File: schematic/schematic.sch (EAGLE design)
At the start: 6 parts, among them IC1 MEGA8-P

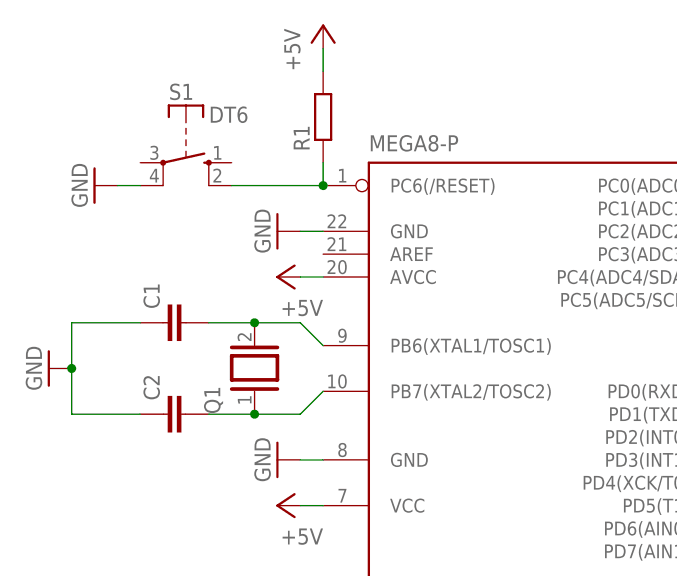
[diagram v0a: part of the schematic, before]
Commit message: Bad at saving schematics - minor update mainly for values
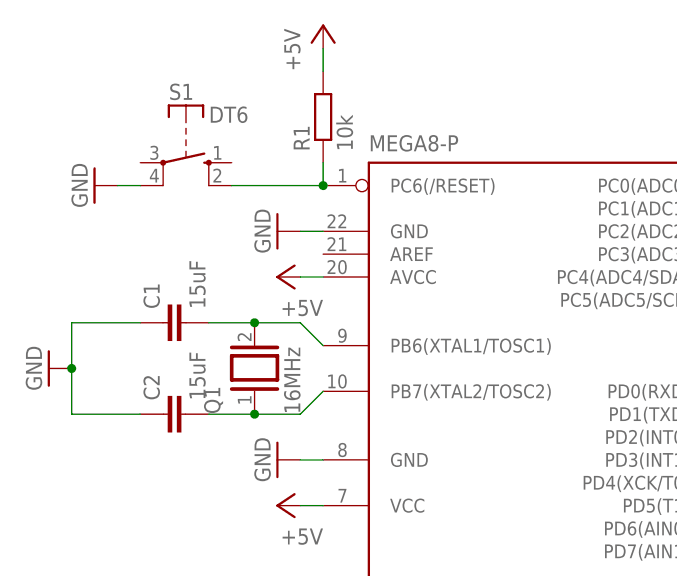
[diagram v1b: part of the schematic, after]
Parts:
- C1, C2: value (none) -> 15uF
- Q1: value (none) -> 16MHz
- R1: value (none) -> 10k
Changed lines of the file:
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@@
 <part name="GND2" library="supply1" deviceset="GND" device=""/>
 <part name="GND3" library="supply1" deviceset="GND" device=""/>
-<part name="Q1" library="special" deviceset="XTAL" device=""/>
-<part name="C1" library="rcl" deviceset="C-EU" device="025-024X044"/>
-<part name="C2" library="rcl" deviceset="C-EU" device="025-024X044"/>
+<part name="Q1" library="special" deviceset="XTAL" device="" value="16MHz"/>
+<part name="C1" library="rcl" deviceset="C-EU" device="025-024X044" value="15uF"/>
+<part name="C2" library="rcl" deviceset="C-EU" device="025-024X044" value="15uF"/>
 <part name="P+3" library="supply1" deviceset="+5V" device=""/>
 <part name="GND4" library="supply1" deviceset="GND" device=""/>
-<part name="R1" library="rcl" deviceset="R-EU_" device="0204/7"/>
+<part name="R1" library="rcl" deviceset="R-EU_" device="0204/7" value="10k"/>
 <part name="S1" library="switch-misc" deviceset="DT" device="6"/>
 </parts>

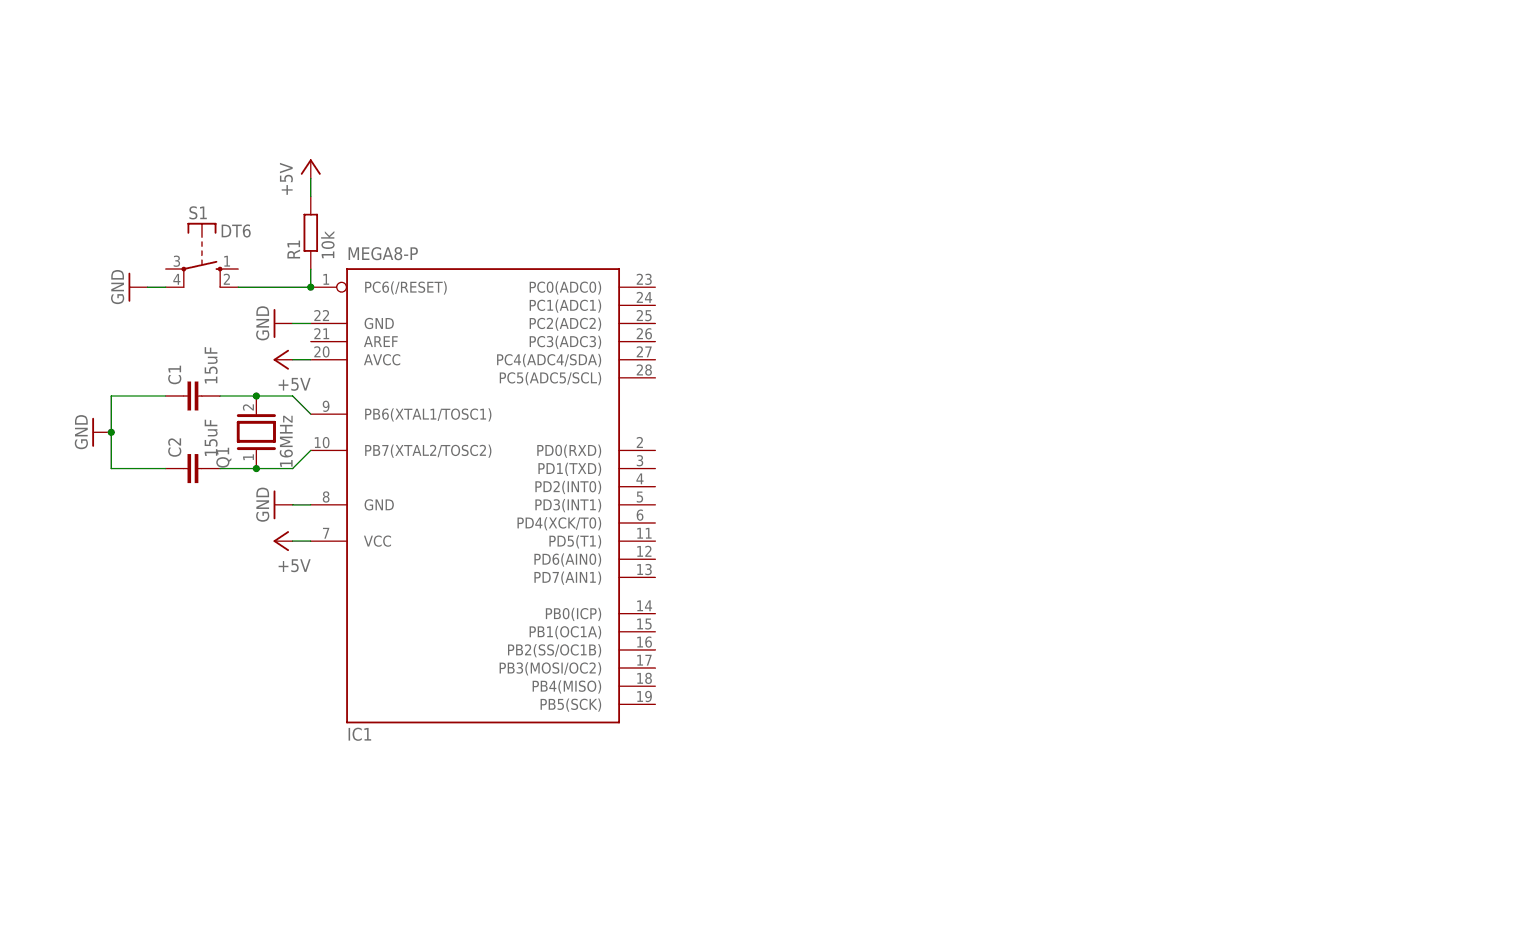
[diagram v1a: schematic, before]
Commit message: Voltage change, Add a host of new subsystems
Critical change: 5V to 3V3, which is slightly out of ratings for 16MHz

Additionally:
* Input buttons
* ICSP Header
* Expansion Header
* SD Card
* Labels
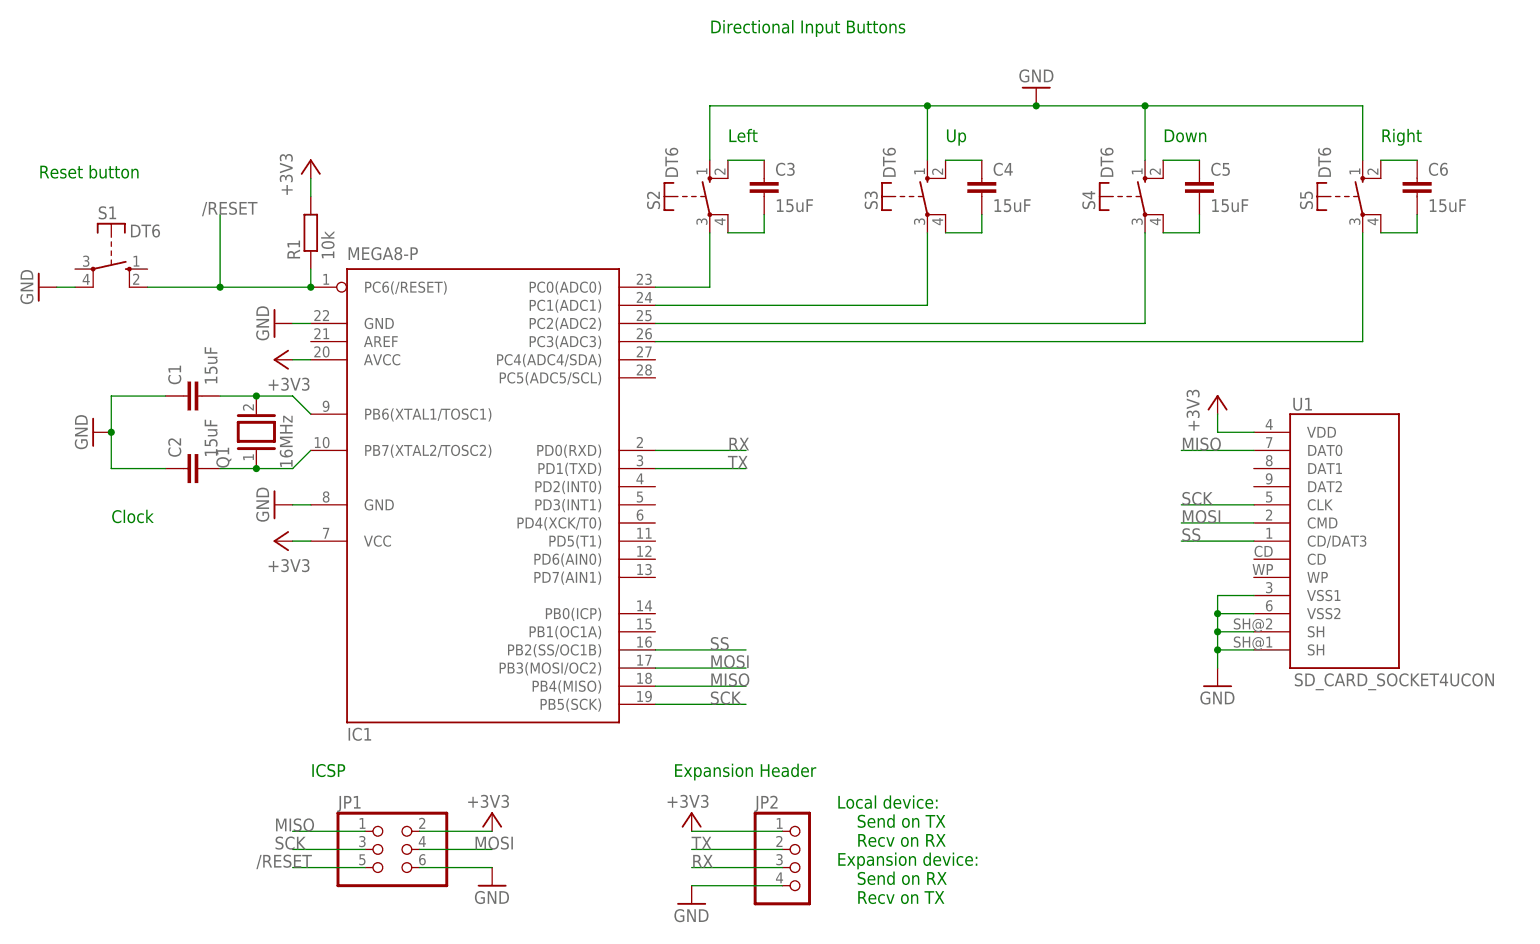
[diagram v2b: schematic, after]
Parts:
- added C3, C4, C5, C6: 15uF, rcl:C-EU025-024X044
- added JP1: (no value), pinhead:PINHD-2X3
- added JP2: (no value), pinhead:PINHD-1X4
- added S2, S3, S4, S5: DT6, switch-misc:DT6
- added U1: SD_CARD_SOCKET4UCON, sfe:SD_CARD_SOCKET4UCON
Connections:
- removed net +5V: IC1.AVCC, IC1.VCC@1, R1.2
- removed net N$3: IC1.PC6(/RESET), R1.1, S1.S@1
- new net +3V3: IC1.AVCC, IC1.VCC@1, JP1.2, JP2.1, R1.2, U1.VDD
- new net /RESET: IC1.PC6(/RESET), JP1.5, R1.1, S1.S@1
- new net MISO: IC1.PB4(MISO), JP1.1, U1.DAT0
- new net MOSI: IC1.PB3(MOSI/OC2), JP1.4, U1.CMD
- new net N$10: C5.1, S4.S@1
- new net N$11: C6.1, S5.S@1
- new net N$12: IC1.PC0(ADC0), S2.P
- new net N$13: IC1.PC1(ADC1), S3.P
- new net N$14: IC1.PC2(ADC2), S4.P
- new net N$15: IC1.PC3(ADC3), S5.P
- new net N$4: C3.2, S2.P@1
- new net N$5: C4.2, S3.P@1
- new net N$6: C5.2, S4.P@1
- new net N$7: C6.2, S5.P@1
- new net N$8: C3.1, S2.S@1
- new net N$9: C4.1, S3.S@1
- new net RX: IC1.PD0(RXD), JP2.3
- new net SCK: IC1.PB5(SCK), JP1.3, U1.CLK
- new net SS: IC1.PB2(SS/OC1B), U1.CD/DAT3
- new net TX: IC1.PD1(TXD), JP2.2
- net GND: now also JP1.6, JP2.4, S2.S, S3.S, S4.S, S5.S, U1.SH@1, U1.SH@2, U1.VSS1, U1.VSS2
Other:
- note added: "Clock"
- note added: "Directional Input Buttons"
- note added: "Down"
- note added: "Expansion Header"
- note added: "ICSP"
- note added: "Left"
- note added: "Local device: Send on TX Recv on RX Expansion device: Send on RX Recv on TX"
- note added: "Reset button"
- note added: "Right"
- note added: "Up"
- moved on the sheet: S1
